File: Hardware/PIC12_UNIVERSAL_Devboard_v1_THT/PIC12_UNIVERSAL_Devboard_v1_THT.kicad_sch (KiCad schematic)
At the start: 0 parts

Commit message: PIC12 Universal Dev Board - Added PIC12, Headers, Power and Status LED Screw Terminal and Reset Switch to Schematics
Signed-off-by: alexanderjg85 <alexanderjg85@gmail.com>
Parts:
- added D1: SS14, Diode_SMD:D_SMA_Handsoldering, symbol Diode:SS14
- added D2: GREEN, LED_SMD:LED_1206_3216Metric_Pad1.42x1.75mm_HandSolder, symbol Device:LED
- added D3: YELLOW, LED_SMD:LED_1206_3216Metric_Pad1.42x1.75mm_HandSolder, symbol Device:LED
- added J1: Conn_01x06_Pin, Connector_PinHeader_2.54mm:PinHeader_1x06_P2.54mm_Vertical, symbol Connector:Conn_01x06_Pin
- added J2: Conn_PIC_ICSP_ICD, Connector_PinHeader_2.54mm:PinHeader_1x06_P2.54mm_Horizontal, symbol Connector:Conn_PIC_ICSP_ICD
- added J3: Screw_Terminal_01x02, TerminalBlock_Phoenix:TerminalBlock_Phoenix_MKDS-1,5-2-5.08_1x02_P5.08mm_Horizontal, symbol Connector:Screw_Terminal_01x02
- added JP1: JP_PLED, TestPoint:TestPoint_2Pads_Pitch2.54mm_Drill0.8mm, symbol Jumper:Jumper_2_Small_Open
- added R1: 680, Resistor_SMD:R_1206_3216Metric_Pad1.30x1.75mm_HandSolder, symbol Device:R_Small
- added R2: 10k, Resistor_SMD:R_1206_3216Metric_Pad1.30x1.75mm_HandSolder, symbol Device:R_Small
- added R3: 330, Resistor_SMD:R_1206_3216Metric_Pad1.30x1.75mm_HandSolder, symbol Device:R_Small
- added SW1: SW_RESET, Button_Switch_SMD:SW_SPST_PTS647_Sx38, symbol Switch:SW_Push
- added TP2: LED, TestPoint:TestPoint_Pad_D1.5mm, symbol Connector:TestPoint
- added U1: PIC12F617-xP, Package_DIP:DIP-8_W7.62mm, symbol MCU_Microchip_PIC12:PIC12F617-xP
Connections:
- new net: D2.2 (A), R1.2
- new net: D1.2 (A), J3.1 (Pin_1)
- new net: D3.2 (A), R3.2
- new net: JP1.1 (A), R3.1
- new net GND: D2.1 (K), D3.1 (K), SW1.2
- new net PIC_LED: R1.1, TP2.1
- new net PIC_RST: R2.2, SW1.1
- new net VCC: R2.1
- new net VDD: JP1.2 (B)

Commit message: PIC12 Universal Dev Board - Schematics - Changed Footprint of the LEDs
Signed-off-by: alexanderjg85 <alexanderjg85@gmail.com>
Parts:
- D2, D3: footprint LED_SMD:LED_1206_3216Metric_Pad1.42x1.75mm_HandSolder -> LED_THT:LED_D3.0mm
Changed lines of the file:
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@@
 			)
 		)
-		(property "Footprint" "LED_SMD:LED_1206_3216Metric_Pad1.42x1.75mm_HandSolder"
+		(property "Footprint" "LED_THT:LED_D3.0mm"
 			(at 102.87 68.58 0)
 			(hide yes)
@@
 			)
 		)
-		(property "Footprint" "LED_SMD:LED_1206_3216Metric_Pad1.42x1.75mm_HandSolder"
+		(property "Footprint" "LED_THT:LED_D3.0mm"
 			(at 160.02 129.54 0)
 			(hide yes)

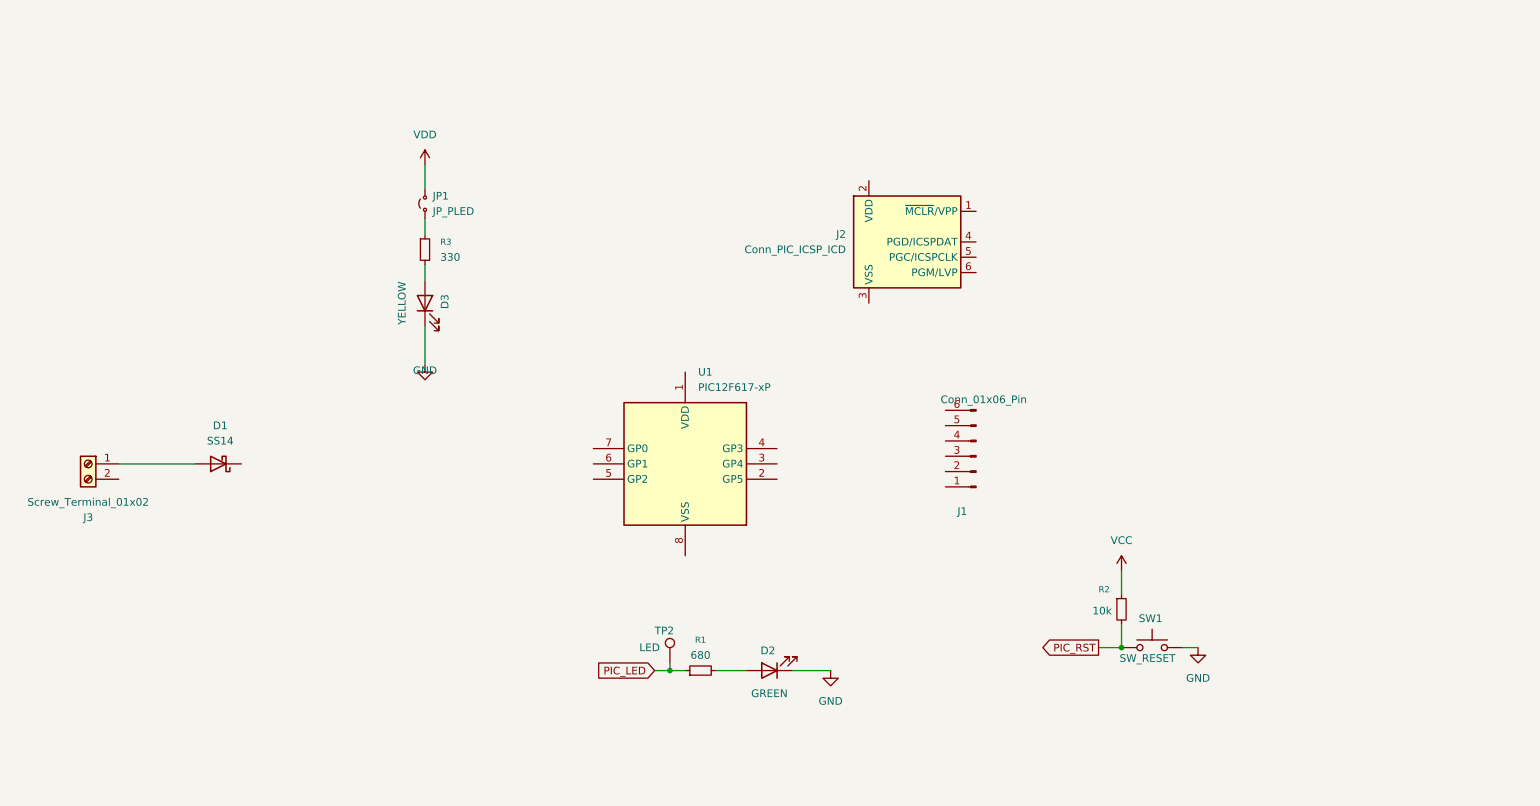
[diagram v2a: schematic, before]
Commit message: PIC12 Universal Dev Board - Schematics - Added remaining components
Signed-off-by: alexanderjg85 <alexanderjg85@gmail.com>
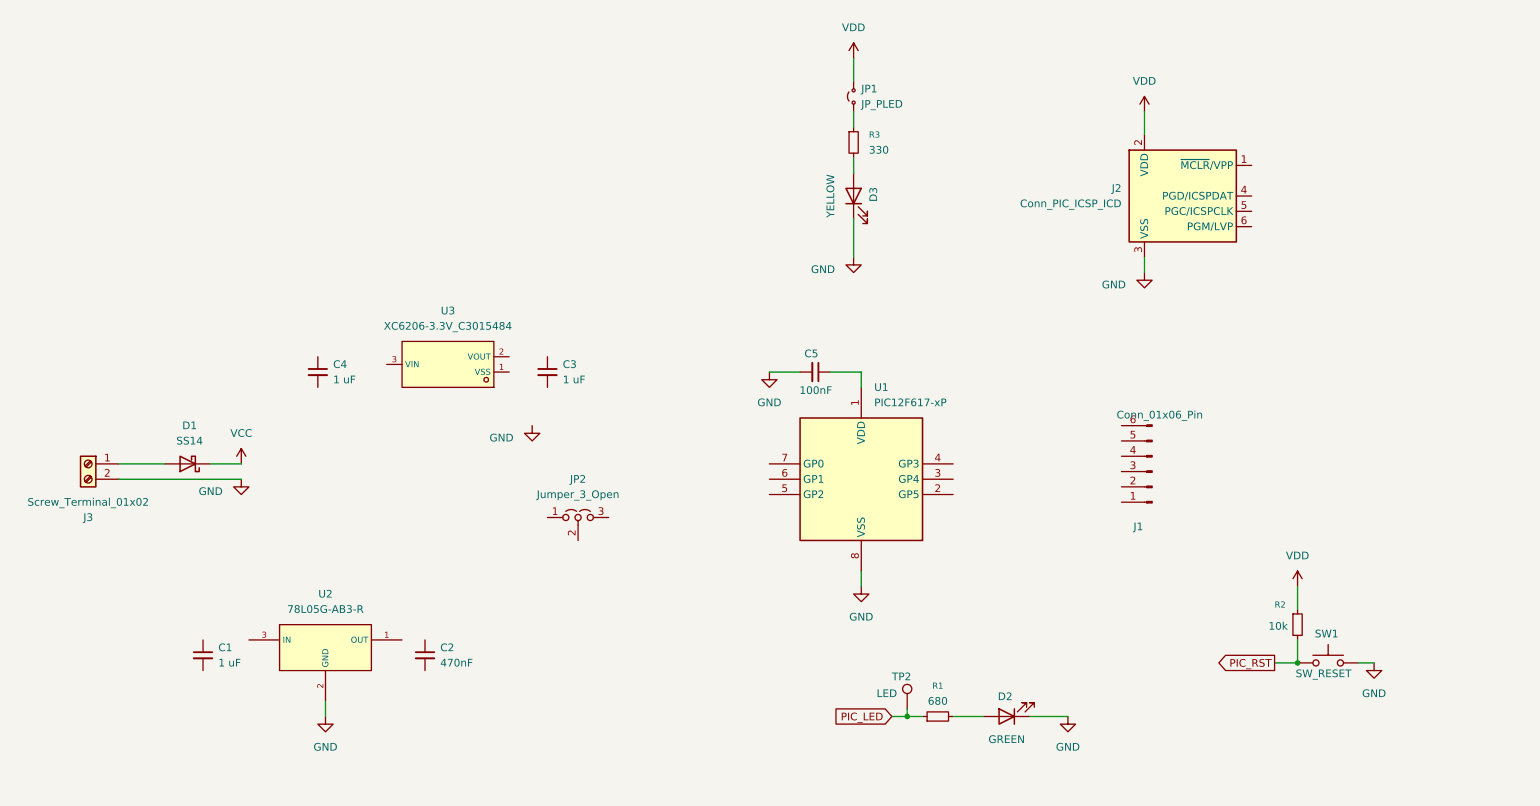
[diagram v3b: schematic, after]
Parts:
- added C1, C3, C4: 1 uF, AJ_Passives:C6119929_C0805, symbol Device:C_Small
- added C2: 470nF, AJ_Passives:C13967_C0805, symbol Device:C_Small
- added C5: 100nF, AJ_Passives:C49678_C0805, symbol Device:C_Small
- added JP2: Jumper_3_Open, symbol Jumper:Jumper_3_Open
- added U2: 78L05G-AB3-R, AJ_Power:C71136_SOT-89-3_L4_5-W2_5-P1_50-LS4_2-BR, symbol AJ_Power:78L05G-AB3-R
- added U3: XC6206-3.3V_C3015484, AJ_Power:C3015484_SOT-23-3_L2_9-W1_3-P0_95-LS2_4-BR, symbol AJ_Power:XC6206-3_3V_C3015484
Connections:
- net GND: now also J2.3 (VSS), J3.2 (Pin_2), U1.8 (VSS), C5.2, U2.2 (GND)
- net VCC: now also D1.1 (K); no longer R2.1
- net VDD: now also J2.2 (VDD), R2.1
- net at U1.1 (VDD): now also C5.1
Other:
- moved on the sheet: D1, D2, D3, J1, J2, JP1, R1, R2, R3, SW1, TP2, U1

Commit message: PIC12 Universal Dev Board - Schematics - Finished Schematics
Signed-off-by: alexanderjg85 <alexanderjg85@gmail.com>
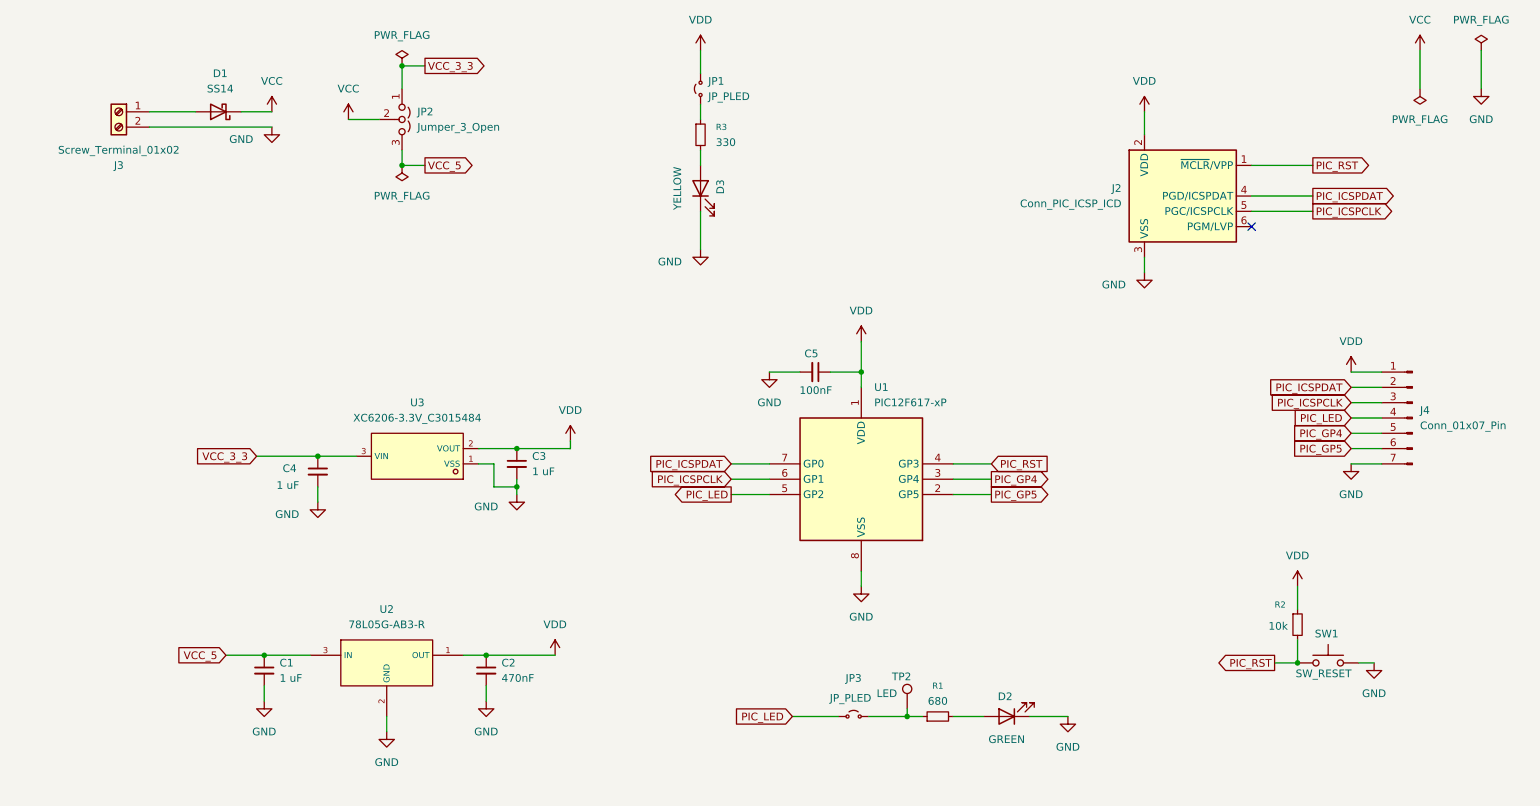
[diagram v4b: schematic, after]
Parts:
- removed J1: Conn_01x06_Pin, Connector_PinHeader_2.54mm:PinHeader_1x06_P2.54mm_Vertical, symbol Connector:Conn_01x06_Pin
- added J4: Conn_01x07_Pin, Connector_PinHeader_2.54mm:PinHeader_1x07_P2.54mm_Vertical, symbol Connector:Conn_01x07_Pin
- added JP3: JP_PLED, TestPoint:TestPoint_2Pads_Pitch2.54mm_Drill0.8mm, symbol Jumper:Jumper_2_Small_Open
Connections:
- net GND: now also C1.2, C2.2, C3.2, C4.2, U3.1 (VSS), J4.7 (Pin_7)
- net PIC_LED: now also U1.5 (GP2), J4.4 (Pin_4), JP3.1 (A); no longer R1.1, TP2.1
- net PIC_RST: now also J2.1 (~{MCLR}/VPP), U1.4 (GP3)
- net VCC: now also JP2.2 (C)
- net VDD: now also C2.1, C3.1, C5.1, U1.1 (VDD), U2.1 (OUT), U3.2 (VOUT), J4.1 (Pin_1)
- net VCC_5: now reaches U2.3 (IN)
- net VCC_5: now also C1.1, JP2.3 (B)
- net VCC_3_3: now reaches JP2.1 (A)
- net VCC_3_3: now also C4.1, U3.3 (VIN)
- net PIC_ICSPDAT: now reaches J2.4 (PGD/ICSPDAT)
- net PIC_ICSPDAT: now also U1.7 (GP0), J4.2 (Pin_2)
- net PIC_ICSPCLK: now reaches J2.5 (PGC/ICSPCLK)
- net PIC_ICSPCLK: now also U1.6 (GP1), J4.3 (Pin_3)
- net PIC_GP5: now reaches U1.2 (GP5)
- net PIC_GP5: now also J4.6 (Pin_6)
- net PIC_GP4: now reaches U1.3 (GP4)
- net PIC_GP4: now also J4.5 (Pin_5)
- new net: JP3.2 (B), R1.1, TP2.1
- no-connect marks 0 -> 1
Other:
- moved on the sheet: C1, C2, C3, C4, D1, D3, J3, JP1, JP2, R3, U2, U3

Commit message: PIC12 Universal Dev Board - Schematics - Added Testpoints
Signed-off-by: alexanderjg85 <alexanderjg85@gmail.com>
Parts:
- added TP1: VDD, TestPoint:TestPoint_Pad_D1.5mm, symbol Connector:TestPoint
- added TP10: GP4, TestPoint:TestPoint_Pad_D1.5mm, symbol Connector:TestPoint
- added TP11: GP5, TestPoint:TestPoint_Pad_D1.5mm, symbol Connector:TestPoint
- added TP3: VCC, TestPoint:TestPoint_Pad_D1.5mm, symbol Connector:TestPoint
- added TP4: VCC3_3, TestPoint:TestPoint_Pad_D1.5mm, symbol Connector:TestPoint
- added TP5: VCC5, TestPoint:TestPoint_Pad_D1.5mm, symbol Connector:TestPoint
- added TP6: GND, TestPoint:TestPoint_Pad_D1.5mm, symbol Connector:TestPoint
- added TP7: DAT, TestPoint:TestPoint_Pad_D1.5mm, symbol Connector:TestPoint
- added TP8: CLK, TestPoint:TestPoint_Pad_D1.5mm, symbol Connector:TestPoint
- added TP9: LED, TestPoint:TestPoint_Pad_D1.5mm, symbol Connector:TestPoint
- TP2: value LED -> PLED
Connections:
- net GND: now also TP6.1
- net PIC_GP4: now also TP10.1
- net PIC_GP5: now also TP11.1
- net PIC_ICSPCLK: now also TP8.1
- net PIC_ICSPDAT: now also TP7.1
- net PIC_LED: now also TP9.1
- net VCC: now also TP3.1
- net VCC_3_3: now also TP4.1
- net VCC_5: now also TP5.1
- net VDD: now also TP1.1
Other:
- moved on the sheet: JP2

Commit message: PIC12 Universal Dev Board - Schematics - Added Footprint for Jumper2
Signed-off-by: alexanderjg85 <alexanderjg85@gmail.com>
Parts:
- JP2: footprint (none) -> Connector_PinHeader_2.54mm:PinHeader_1x03_P2.54mm_Vertical
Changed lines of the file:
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@@
 			)
 		)
-		(property "Footprint" ""
+		(property "Footprint" "Connector_PinHeader_2.54mm:PinHeader_1x03_P2.54mm_Vertical"
 			(at 111.76 38.1 0)
 			(hide yes)

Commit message: PIC12 Universal Dev Board - Schematics - Changed Footprint of ICSP Header Layout - Defined Egde Cut, Imported Components from schematics
Signed-off-by: alexanderjg85 <alexanderjg85@gmail.com>
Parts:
- J2: footprint Connector_PinHeader_2.54mm:PinHeader_1x06_P2.54mm_Horizontal -> Connector_PinHeader_2.54mm:PinHeader_1x06_P2.54mm_Vertical
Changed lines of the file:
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@@
 			)
 		)
-		(property "Footprint" "Connector_PinHeader_2.54mm:PinHeader_1x06_P2.54mm_Horizontal"
+		(property "Footprint" "Connector_PinHeader_2.54mm:PinHeader_1x06_P2.54mm_Vertical"
 			(at 228.6 46.99 0)
 			(hide yes)

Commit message: PIC12 Universal Dev Board - Schematics - Added Reverse Current Protection Diode for 78L05 Regulator
Signed-off-by: alexanderjg85 <alexanderjg85@gmail.com>
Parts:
- added D4: SS14, Diode_SMD:D_SMA_Handsoldering, symbol Diode:SS14
- JP3: value JP_PLED -> JP_SLED
- TP2: value PLED -> SLED
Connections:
- net VCC_5: now also D4.1 (K)
- net VDD: now also D4.2 (A)
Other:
- moved on the sheet: C1, C2, C3, C4, TP4, TP5, U2, U3
